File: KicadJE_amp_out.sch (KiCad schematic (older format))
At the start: 10 parts

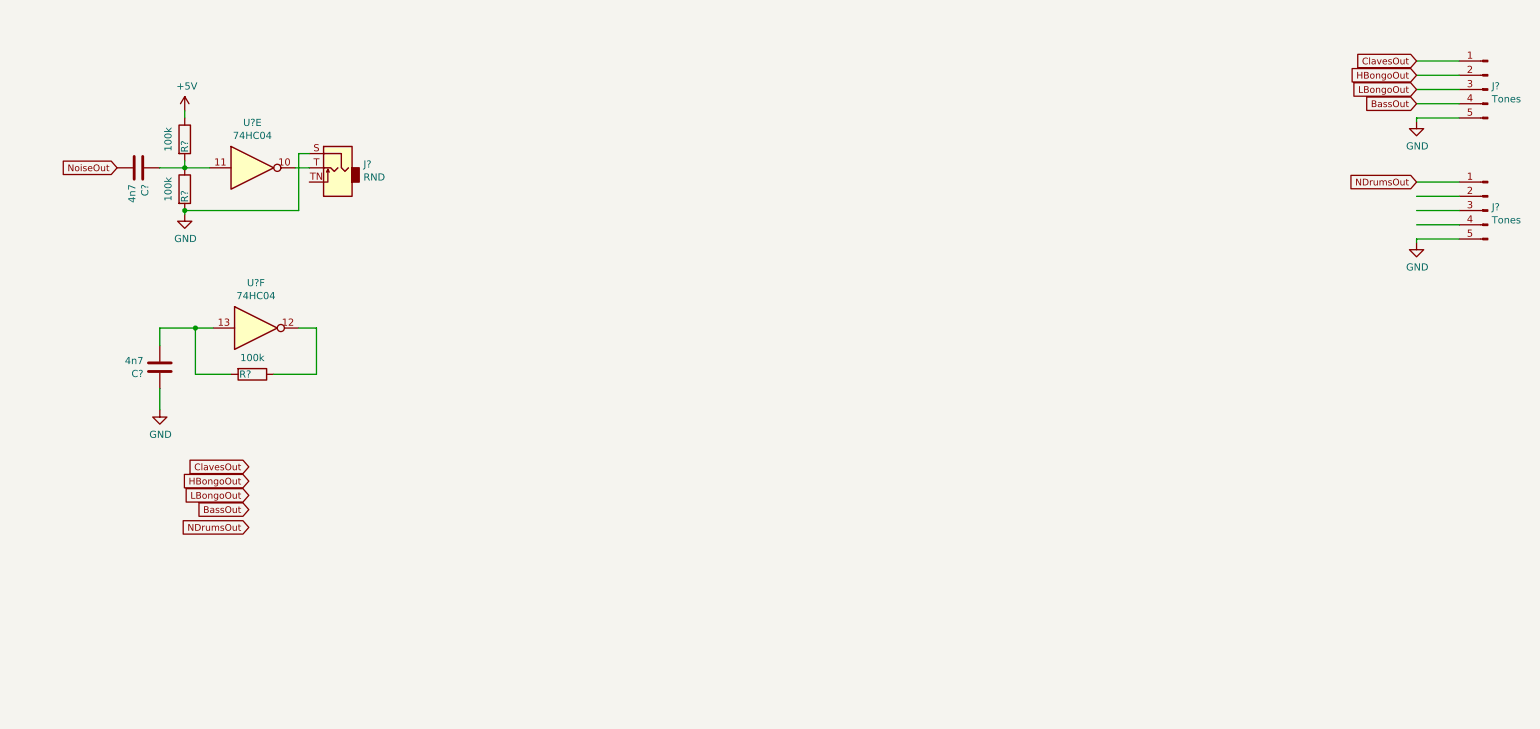
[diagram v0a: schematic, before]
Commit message: Amp out
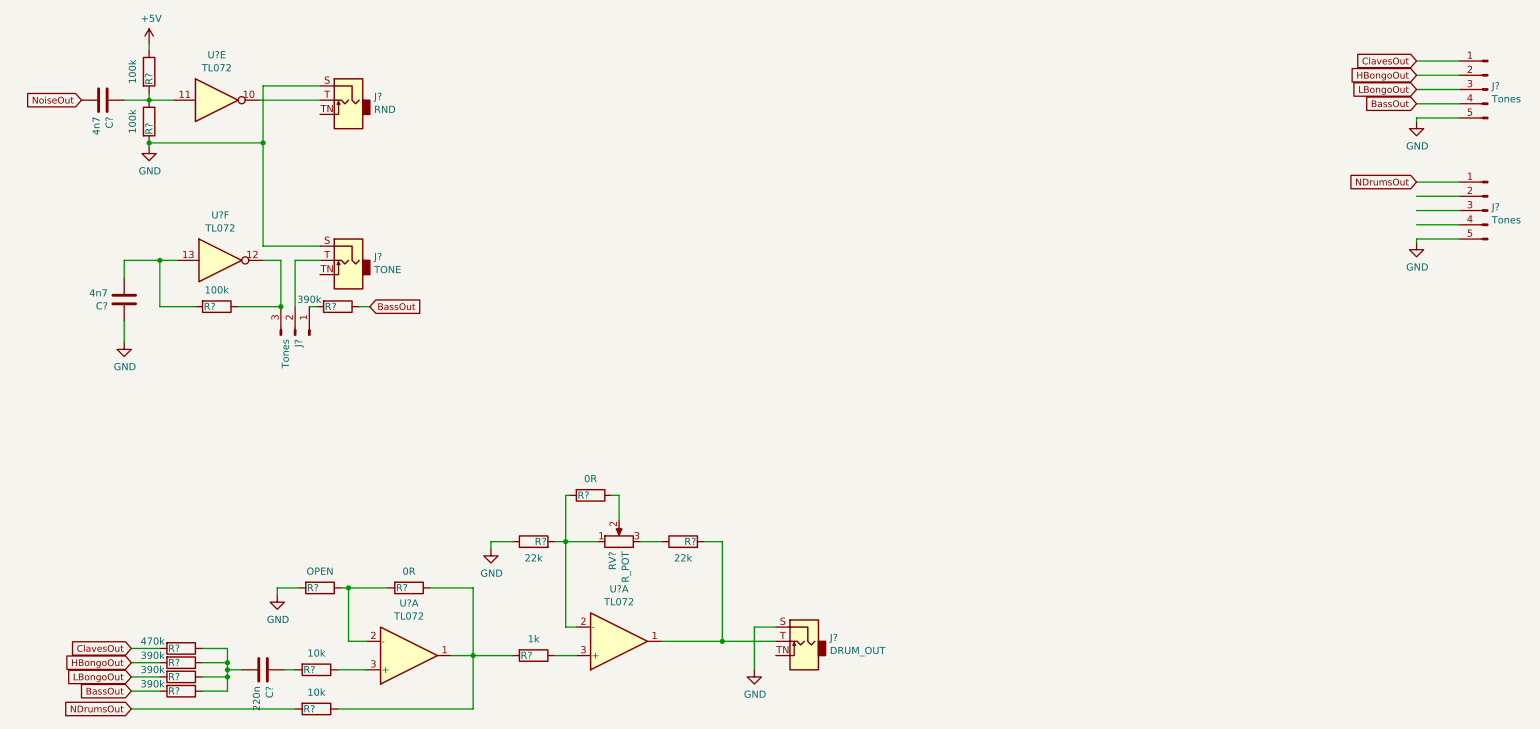
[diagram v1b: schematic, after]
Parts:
- added C?: 220n, Capacitor_SMD:C_1206_3216Metric_Pad1.42x1.75mm_HandSolder, symbol Device:C
- added J?: TONE, Connector_Audio:Jack_3.5mm_QingPu_WQP-PJ398SM_Vertical_CircularHoles, symbol Connector:AudioJack2_SwitchT
- added J?: Tones, Connector_PinHeader_2.54mm:PinHeader_1x03_P2.54mm_Vertical, symbol Connector:Conn_01x03_Male
- added J?: DRUM_OUT, Connector_Audio:Jack_3.5mm_QingPu_WQP-PJ398SM_Vertical_CircularHoles, symbol Connector:AudioJack2_SwitchT
- added R? (x4): 390k, AJ:R_0805_AJ, symbol Device:R
- added R?: 470k, AJ:R_0805_AJ, symbol Device:R
- added R? (x2): 10k, AJ:R_0805_AJ, symbol Device:R
- added R? (x2): 22k, AJ:R_0805_AJ, symbol Device:R
- added R?: 1k, AJ:R_0805_AJ, symbol Device:R
- added R? (x2): 0R, AJ:R_0805_AJ, symbol Device:R
- added R?: OPEN, AJ:R_0805_AJ, symbol Device:R
- added RV?: R_POT, AJ:Potentiometer_China_RK09_Single_Vertical_AJ, symbol Device:R_POT
- added U? (x2): TL072, AJ:AJ_SO-8_5.3x6.2mm_P1.27mm, symbol Amplifier_Operational:TL072
- U? (x2): value 74HC04 -> TL072; footprint (none) -> AJ:AJ_SO-8_5.3x6.2mm_P1.27mm
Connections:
- wire segments 30 -> 82
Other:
- moved on the sheet: C?, J?, R?, U?E, U?F

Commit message: sch amp
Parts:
- R?: value 390k -> 10k
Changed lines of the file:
@@
 Wire Wire Line
 	2425 2225 2600 2225
-Text GLabel 2950 2550 2    47   Input ~ 0
-BassOut
 $Comp
 L Device:C C?
@@
 AR Path="/6165D4D0/61BC62DE" Ref="R?"  Part="1"
 F 0 "R?" V 2725 2500 50  0000 C CNN
-F 1 "390k" V 2675 2350 50  0000 C CNN
+F 1 "10k" V 2675 2350 50  0000 C CNN
 F 2 "AJ:R_0805_AJ" V 2655 2550 50  0001 C CNN
 F 3 "~" H 2725 2550 50  0001 C CNN
@@
 Wire Wire Line
 	5650 4800 5650 5100
+Text GLabel 10300 1775 0    47   Input ~ 0
+NoiseOut
+Text GLabel 2950 2550 2    47   Input ~ 0
+NoiseOut
 $EndSCHEMATC

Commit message: Update misc diags
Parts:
- added R? (x3): 390k, AJ:R_0805_AJ, symbol Device:R
- added R?: 470k, AJ:R_0805_AJ, symbol Device:R
- added R? (x2): 10k, AJ:R_0805_AJ, symbol Device:R
- J?: value Tones -> Noise; footprint Connector_PinHeader_2.54mm:PinHeader_1x05_P2.54mm_Vertical -> Connector_PinHeader_2.54mm:PinHeader_1x03_P2.54mm_Vertical; symbol Connector:Conn_01x05_Male -> Connector:Conn_01x03_Male
- J?: value Tones -> Tone/Noise
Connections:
- net BassOut: now also R?.2; no longer J?.4 (Pin_4)
- net ClavesOut: now also R?.2; no longer J?.1 (Pin_1)
- net GND: now also J?.1 (Pin_1), J?.1 (Pin_1); no longer J?.5 (Pin_5), J?.5 (Pin_5)
- net HBongoOut: now also R?.2; no longer J?.2 (Pin_2)
- net LBongoOut: now also R?.2; no longer J?.3 (Pin_3)
- net NDrumsOut: now also R?.2; no longer J?.1 (Pin_1)
- net NoiseOut: now also R?.2; no longer J?.2 (Pin_2)
- net at J?.3 (Pin_3): now also R?.1
- new net: J?.4 (Pin_4), R?.1
- new net: J?.5 (Pin_5), R?.1
- new net: J?.3 (Pin_3), R?.1
- new net: J?.2 (Pin_2), R?.1 (x2)
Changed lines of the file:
@@
 F 3 "~" H 10800 1025 50  0001 C CNN
 	1    10800 1025
-	-1   0    0    -1
-$EndComp
-Text GLabel 10300 1025 0    47   Input ~ 0
+	-1   0    0    1
+$EndComp
+Text GLabel 9800 1025 0    47   Input ~ 0
 LBongoOut
-Text GLabel 10300 1125 0    47   Input ~ 0
+Text GLabel 9800 1125 0    47   Input ~ 0
 BassOut
-Text GLabel 10300 825  0    47   Input ~ 0
+Text GLabel 9800 825  0    47   Input ~ 0
 ClavesOut
-Text GLabel 10300 925  0    47   Input ~ 0
+Text GLabel 9800 925  0    47   Input ~ 0
 HBongoOut
 Wire Wire Line
@@
 	2325 2225 2200 2225
 $Comp
-L Connector:Conn_01x05_Male J?
+L Connector:Conn_01x03_Male J?
 U 1 1 61710EAB
-P 10800 1875
+P 10800 1775
 AR Path="/607E07E1/61710EAB" Ref="J?"  Part="1"
 AR Path="/61710EAB" Ref="J?"  Part="1"
 AR Path="/6165D4D0/61710EAB" Ref="J?"  Part="1"
-F 0 "J?" H 10772 1899 50  0000 R CNN
-F 1 "Tones" H 10772 1808 50  0000 R CNN
-F 2 "Connector_PinHeader_2.54mm:PinHeader_1x05_P2.54mm_Vertical" H 10800 1875 50  0001 C CNN
-F 3 "~" H 10800 1875 50  0001 C CNN
-	1    10800 1875
-	-1   0    0    -1
+F 0 "J?" V 10772 1799 50  0000 R CNN
+F 1 "Noise" H 10772 1708 50  0000 R CNN
+F 2 "Connector_PinHeader_2.54mm:PinHeader_1x03_P2.54mm_Vertical" H 10800 1775 50  0001 C CNN
+F 3 "~" H 10800 1775 50  0001 C CNN
+	1    10800 1775
+	-1   0    0    1
 $EndComp
 $Comp
 L power:GND #PWR?
 U 1 1 61715219
-P 10300 2100
+P 10300 1900
 AR Path="/61715219" Ref="#PWR?"  Part="1"
 AR Path="/6165D4D0/61715219" Ref="#PWR?"  Part="1"
-F 0 "#PWR?" H 10300 1850 50  0001 C CNN
-F 1 "GND" H 10305 1927 50  0000 C CNN
-F 2 "" H 10300 2100 50  0001 C CNN
-F 3 "" H 10300 2100 50  0001 C CNN
-	1    10300 2100
+F 0 "#PWR?" H 10300 1650 50  0001 C CNN
+F 1 "GND" H 10305 1727 50  0000 C CNN
+F 2 "" H 10300 1900 50  0001 C CNN
+F 3 "" H 10300 1900 50  0001 C CNN
+	1    10300 1900
 	1    0    0    -1
 $EndComp
 Wire Wire Line
-	10300 2100 10300 2075
-Wire Wire Line
-	10300 2075 10600 2075
-Text GLabel 10300 1675 0    47   Input ~ 0
+	10300 1900 10300 1875
+Text GLabel 9800 1675 0    47   Input ~ 0
 NDrumsOut
-Wire Wire Line
-	10600 1975 10300 1975
 Wire Wire Line
 	10300 1875 10600 1875
@@
 AR Path="/6165D4D0/61A8A423" Ref="J?"  Part="1"
 F 0 "J?" H 2397 2774 50  0000 R CNN
-F 1 "Tones" H 2397 2683 50  0000 R CNN
+F 1 "Tone/Noise" H 2397 2683 50  0000 R CNN
 F 2 "Connector_PinHeader_2.54mm:PinHeader_1x03_P2.54mm_Vertical" H 2425 2750 50  0001 C CNN
 F 3 "~" H 2425 2750 50  0001 C CNN
@@
 Wire Wire Line
 	5650 4800 5650 5100
-Text GLabel 10300 1775 0    47   Input ~ 0
+Text GLabel 9800 1775 0    47   Input ~ 0
 NoiseOut
 Text GLabel 2950 2550 2    47   Input ~ 0
 NoiseOut
+$Comp
+L Device:R R?
+U 1 1 608AC9E1
+P 10150 925
+AR Path="/608AC9E1" Ref="R?"  Part="1"
+AR Path="/5C8C5FC0/608AC9E1" Ref="R?"  Part="1"
+AR Path="/5D60ED9A/608AC9E1" Ref="R?"  Part="1"
+AR Path="/60565919/608AC9E1" Ref="R?"  Part="1"
+AR Path="/6165D4D0/608AC9E1" Ref="R?"  Part="1"
+F 0 "R?" V 10150 875 50  0000 C CNN
+F 1 "390k" V 10100 725 50  0000 C CNN
+F 2 "AJ:R_0805_AJ" V 10080 925 50  0001 C CNN
+F 3 "~" H 10150 925 50  0001 C CNN
+	1    10150 925
+	0    1    1    0
+$EndComp
+$Comp
+L Device:R R?
+U 1 1 608ACE07
+P 10150 825
+AR Path="/608ACE07" Ref="R?"  Part="1"
+AR Path="/5C8C5FC0/608ACE07" Ref="R?"  Part="1"
+AR Path="/5D60ED9A/608ACE07" Ref="R?"  Part="1"
+AR Path="/60565919/608ACE07" Ref="R?"  Part="1"
+AR Path="/6165D4D0/608ACE07" Ref="R?"  Part="1"
+F 0 "R?" V 10150 775 50  0000 C CNN
+F 1 "470k" V 10100 625 50  0000 C CNN
+F 2 "AJ:R_0805_AJ" V 10080 825 50  0001 C CNN
+F 3 "~" H 10150 825 50  0001 C CNN
+	1    10150 825
+	0    1    1    0
+$EndComp
+$Comp
+L Device:R R?
+U 1 1 608ACE11
+P 10150 1025
+AR Path="/608ACE11" Ref="R?"  Part="1"
+AR Path="/5C8C5FC0/608ACE11" Ref="R?"  Part="1"
+AR Path="/5D60ED9A/608ACE11" Ref="R?"  Part="1"
+AR Path="/60565919/608ACE11" Ref="R?"  Part="1"
+AR Path="/6165D4D0/608ACE11" Ref="R?"  Part="1"
+F 0 "R?" V 10150 975 50  0000 C CNN
+F 1 "390k" V 10100 825 50  0000 C CNN
+F 2 "AJ:R_0805_AJ" V 10080 1025 50  0001 C CNN
+F 3 "~" H 10150 1025 50  0001 C CNN
+	1    10150 1025
+	0    1    1    0
+$EndComp
+$Comp
+L Device:R R?
+U 1 1 608ACE1B
+P 10150 1125
+AR Path="/608ACE1B" Ref="R?"  Part="1"
+AR Path="/5C8C5FC0/608ACE1B" Ref="R?"  Part="1"
+AR Path="/5D60ED9A/608ACE1B" Ref="R?"  Part="1"
+AR Path="/60565919/608ACE1B" Ref="R?"  Part="1"
+AR Path="/6165D4D0/608ACE1B" Ref="R?"  Part="1"
+F 0 "R?" V 10150 1075 50  0000 C CNN
+F 1 "390k" V 10100 925 50  0000 C CNN
+F 2 "AJ:R_0805_AJ" V 10080 1125 50  0001 C CNN
+F 3 "~" H 10150 1125 50  0001 C CNN
+	1    10150 1125
+	0    1    1    0
+$EndComp
+Wire Wire Line
+	9800 825  10000 825
+Wire Wire Line
+	10000 1125 9800 1125
+Wire Wire Line
+	9800 1025 10000 1025
+Wire Wire Line
+	10000 925  9800 925
+$Comp
+L Device:R R?
+U 1 1 608B8687
+P 10150 1675
+AR Path="/608B8687" Ref="R?"  Part="1"
+AR Path="/5C8C5FC0/608B8687" Ref="R?"  Part="1"
+AR Path="/5D60ED9A/608B8687" Ref="R?"  Part="1"
+AR Path="/60565919/608B8687" Ref="R?"  Part="1"
+AR Path="/6165D4D0/608B8687" Ref="R?"  Part="1"
+F 0 "R?" V 10150 1625 50  0000 C CNN
+F 1 "10k" V 10100 1475 50  0000 C CNN
+F 2 "AJ:R_0805_AJ" V 10080 1675 50  0001 C CNN
+F 3 "~" H 10150 1675 50  0001 C CNN
+	1    10150 1675
+	0    1    1    0
+$EndComp
+$Comp
+L Device:R R?
+U 1 1 608B8FB9
+P 10150 1775
+AR Path="/608B8FB9" Ref="R?"  Part="1"
+AR Path="/5C8C5FC0/608B8FB9" Ref="R?"  Part="1"
+AR Path="/5D60ED9A/608B8FB9" Ref="R?"  Part="1"
+AR Path="/60565919/608B8FB9" Ref="R?"  Part="1"
+AR Path="/6165D4D0/608B8FB9" Ref="R?"  Part="1"
+F 0 "R?" V 10150 1725 50  0000 C CNN
+F 1 "10k" V 10100 1575 50  0000 C CNN
+F 2 "AJ:R_0805_AJ" V 10080 1775 50  0001 C CNN
+F 3 "~" H 10150 1775 50  0001 C CNN
+	1    10150 1775
+	0    1    1    0
+$EndComp
+Wire Wire Line
+	10000 1775 9800 1775
+Wire Wire Line
+	9800 1675 10000 1675
 $EndSCHEMATC

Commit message: Annotate
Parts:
- gave numbers to parts that had none: 35

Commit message: Footprint adj
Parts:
- U101: renamed from U301; value TL072 -> 74HC04; footprint AJ:AJ_SO-8_5.3x6.2mm_P1.27mm -> AJ:AJ_SO-14_5.3x6.2mm_P1.27mm
- renumbered U303 to U302
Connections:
- net at J304.T, R316.2: now also U302.7; no longer U302.1
- net at R313.2, R315.2, RV301.1: now also U302.6 (-); no longer U302.2 (-)
- net at R314.1: now also U302.5 (+); no longer U302.3 (+)
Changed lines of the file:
@@
 P 1875 1100
 AR Path="/61681728" Ref="U?"  Part="5"
-AR Path="/6165D4D0/61681728" Ref="U301"  Part="5"
-F 0 "U301" H 1875 1417 50  0000 C CNN
-F 1 "TL072" H 1875 1326 50  0000 C CNN
-F 2 "AJ:AJ_SO-8_5.3x6.2mm_P1.27mm" H 1875 1100 50  0001 C CNN
-F 3 "http://www.ti.com/lit/ds/symlink/tl071.pdf" H 1875 1100 50  0001 C CNN
+AR Path="/6165D4D0/61681728" Ref="U101"  Part="5"
+F 0 "U101" H 1875 1417 50  0000 C CNN
+F 1 "74HC04" H 1875 1326 50  0000 C CNN
+F 2 "AJ:AJ_SO-14_5.3x6.2mm_P1.27mm" H 1875 1100 50  0001 C CNN
+F 3 "" H 1875 1100 50  0001 C CNN
 	5    1875 1100
 	1    0    0    -1
@@
 P 1900 2225
 AR Path="/6168172E" Ref="U?"  Part="6"
-AR Path="/6165D4D0/6168172E" Ref="U301"  Part="6"
-F 0 "U301" H 1900 2542 50  0000 C CNN
-F 1 "TL072" H 1900 2451 50  0000 C CNN
-F 2 "AJ:AJ_SO-8_5.3x6.2mm_P1.27mm" H 1900 2225 50  0001 C CNN
-F 3 "http://www.ti.com/lit/ds/symlink/tl071.pdf" H 1900 2225 50  0001 C CNN
+AR Path="/6165D4D0/6168172E" Ref="U101"  Part="6"
+F 0 "U101" H 1900 2542 50  0000 C CNN
+F 1 "74HC04" H 1900 2451 50  0000 C CNN
+F 2 "AJ:AJ_SO-14_5.3x6.2mm_P1.27mm" H 1900 2225 50  0001 C CNN
+F 3 "" H 1900 2225 50  0001 C CNN
 	6    1900 2225
 	1    0    0    -1
@@
 	3675 5000 3525 5000
 $Comp
-L Amplifier_Operational:TL072 U303
-U 1 1 61BAEFD9
+L Amplifier_Operational:TL072 U302
+U 2 1 61BAEFD9
 P 4700 4900
-F 0 "U303" H 4700 4533 50  0000 C CNN
+F 0 "U302" H 4700 4533 50  0000 C CNN
 F 1 "TL072" H 4700 4624 50  0000 C CNN
 F 2 "AJ:AJ_SO-8_5.3x6.2mm_P1.27mm" H 4700 4900 50  0001 C CNN
 F 3 "http://www.ti.com/lit/ds/symlink/tl071.pdf" H 4700 4900 50  0001 C CNN
-	1    4700 4900
+	2    4700 4900
 	1    0    0    1
 $EndComp

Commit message: Faceplate etc
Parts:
- U101: footprint AJ:AJ_SO-14_5.3x6.2mm_P1.27mm -> Package_SO:SO-14_5.3x10.2mm_P1.27mm
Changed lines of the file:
@@
 F 0 "U101" H 1875 1417 50  0000 C CNN
 F 1 "74HC04" H 1875 1326 50  0000 C CNN
-F 2 "AJ:AJ_SO-14_5.3x6.2mm_P1.27mm" H 1875 1100 50  0001 C CNN
+F 2 "Package_SO:SO-14_5.3x10.2mm_P1.27mm" H 1875 1100 50  0001 C CNN
 F 3 "" H 1875 1100 50  0001 C CNN
 	5    1875 1100
@@
 F 0 "U101" H 1900 2542 50  0000 C CNN
 F 1 "74HC04" H 1900 2451 50  0000 C CNN
-F 2 "AJ:AJ_SO-14_5.3x6.2mm_P1.27mm" H 1900 2225 50  0001 C CNN
+F 2 "Package_SO:SO-14_5.3x10.2mm_P1.27mm" H 1900 2225 50  0001 C CNN
 F 3 "" H 1900 2225 50  0001 C CNN
 	6    1900 2225

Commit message: Powerfootprintupdated
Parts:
- removed R315: 0R, AJ:R_0805_AJ, symbol Device:R
- removed RV301: R_POT, AJ:Potentiometer_China_RK09_Single_Vertical_AJ, symbol Device:R_POT
- C301, C302, C303: footprint Capacitor_SMD:C_1206_3216Metric_Pad1.42x1.75mm_HandSolder -> AJ:C_0805_AJ
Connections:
- net at R313.2, U302.6 (-): now also R316.1
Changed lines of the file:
@@
 F 0 "C301" H 1190 1146 50  0000 L CNN
 F 1 "4n7" H 1190 1055 50  0000 L CNN
-F 2 "Capacitor_SMD:C_1206_3216Metric_Pad1.42x1.75mm_HandSolder" H 1113 950 50  0001 C CNN
+F 2 "AJ:C_0805_AJ" H 1113 950 50  0001 C CNN
 F 3 "~" H 1075 1100 50  0001 C CNN
 	1    1075 1100
@@
 F 0 "C302" H 1340 2546 50  0000 L CNN
 F 1 "4n7" H 1340 2455 50  0000 L CNN
-F 2 "Capacitor_SMD:C_1206_3216Metric_Pad1.42x1.75mm_HandSolder" H 1263 2350 50  0001 C CNN
+F 2 "AJ:C_0805_AJ" H 1263 2350 50  0001 C CNN
 F 3 "~" H 1225 2500 50  0001 C CNN
 	1    1225 2500
@@
 F 0 "C303" H 2315 5146 50  0000 L CNN
 F 1 "220n" H 2315 5055 50  0000 L CNN
-F 2 "Capacitor_SMD:C_1206_3216Metric_Pad1.42x1.75mm_HandSolder" H 2238 4950 50  0001 C CNN
+F 2 "AJ:C_0805_AJ" H 2238 4950 50  0001 C CNN
 F 3 "~" H 2200 5100 50  0001 C CNN
 	1    2200 5100
@@
 	0    -1   -1   0
 $EndComp
-$Comp
-L Device:R_POT RV301
-U 1 1 61BB7D8E
-P 4700 4200
-F 0 "RV301" H 4631 4246 50  0000 R CNN
-F 1 "R_POT" H 4631 4155 50  0000 R CNN
-F 2 "AJ:Potentiometer_China_RK09_Single_Vertical_AJ" H 4700 4200 50  0001 C CNN
-F 3 "~" H 4700 4200 50  0001 C CNN
-	1    4700 4200
-	0    -1   -1   0
-$EndComp
 Wire Wire Line
 	5425 4200 5300 4200
@@
 	4325 4800 4325 4200
 Wire Wire Line
-	4325 4200 4550 4200
-Wire Wire Line
-	4850 4200 5000 4200
-Wire Wire Line
 	4325 4200 4250 4200
-Connection ~ 4325 4200
 Wire Wire Line
 	5000 4900 5425 4900
@@
 	2300 4525 2450 4525
 $Comp
-L Device:R R?
-U 1 1 61BE0178
-P 4500 3875
-AR Path="/61BE0178" Ref="R?"  Part="1"
-AR Path="/5C8C5FC0/61BE0178" Ref="R?"  Part="1"
-AR Path="/5D60ED9A/61BE0178" Ref="R?"  Part="1"
-AR Path="/60565919/61BE0178" Ref="R?"  Part="1"
-AR Path="/6165D4D0/61BE0178" Ref="R315"  Part="1"
-F 0 "R315" V 4500 3825 50  0000 C CNN
-F 1 "0R" V 4384 3875 50  0000 C CNN
-F 2 "AJ:R_0805_AJ" V 4430 3875 50  0001 C CNN
-F 3 "~" H 4500 3875 50  0001 C CNN
-	1    4500 3875
-	0    1    1    0
-$EndComp
-Wire Wire Line
-	4700 4050 4700 3875
-Wire Wire Line
-	4700 3875 4650 3875
-Wire Wire Line
-	4325 3875 4325 4200
-Wire Wire Line
-	4350 3875 4325 3875
-$Comp
 L Connector:AudioJack2_SwitchT J?
 U 1 1 61BE2ABB
@@
 Wire Wire Line
 	9800 1675 10000 1675
+Wire Wire Line
+	4325 4200 5000 4200
+Connection ~ 4325 4200
 $EndSCHEMATC

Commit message: AC coupled noise
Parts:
- added C304: 220n, AJ:C_0805_AJ, symbol Device:C
- J303: value TONE -> Noise
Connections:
- net at J303.T: now also C304.1; no longer J301.2 (Pin_2)
- new net: C304.2, J301.2 (Pin_2)
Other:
- moved on the sheet: J302, J303
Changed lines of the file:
@@
 L Connector:AudioJack2_SwitchT J?
 U 1 1 61681759
-P 2800 1100
+P 3250 1100
 AR Path="/607E07E1/61681759" Ref="J?"  Part="1"
 AR Path="/61681759" Ref="J?"  Part="1"
 AR Path="/6165D4D0/61681759" Ref="J302"  Part="1"
-F 0 "J302" H 2620 1125 50  0000 R CNN
-F 1 "RND" H 2620 1034 50  0000 R CNN
-F 2 "Connector_Audio:Jack_3.5mm_QingPu_WQP-PJ398SM_Vertical_CircularHoles" H 2800 1100 50  0001 C CNN
-F 3 "~" H 2800 1100 50  0001 C CNN
-	1    2800 1100
+F 0 "J302" H 3070 1125 50  0000 R CNN
+F 1 "RND" H 3070 1034 50  0000 R CNN
+F 2 "Connector_Audio:Jack_3.5mm_QingPu_WQP-PJ398SM_Vertical_CircularHoles" H 3250 1100 50  0001 C CNN
+F 3 "~" H 3250 1100 50  0001 C CNN
+	1    3250 1100
 	-1   0    0    -1
 $EndComp
@@
 L Connector:AudioJack2_SwitchT J?
 U 1 1 61A8618F
-P 2800 2225
+P 3250 2225
 AR Path="/607E07E1/61A8618F" Ref="J?"  Part="1"
 AR Path="/61A8618F" Ref="J?"  Part="1"
 AR Path="/6165D4D0/61A8618F" Ref="J303"  Part="1"
-F 0 "J303" H 2620 2250 50  0000 R CNN
-F 1 "TONE" H 2620 2159 50  0000 R CNN
-F 2 "Connector_Audio:Jack_3.5mm_QingPu_WQP-PJ398SM_Vertical_CircularHoles" H 2800 2225 50  0001 C CNN
-F 3 "~" H 2800 2225 50  0001 C CNN
-	1    2800 2225
+F 0 "J303" H 3070 2250 50  0000 R CNN
+F 1 "Noise" H 3070 2159 50  0000 R CNN
+F 2 "Connector_Audio:Jack_3.5mm_QingPu_WQP-PJ398SM_Vertical_CircularHoles" H 3250 2225 50  0001 C CNN
+F 3 "~" H 3250 2225 50  0001 C CNN
+	1    3250 2225
 	-1   0    0    -1
 $EndComp
-Wire Wire Line
-	2200 1000 2600 1000
-Wire Wire Line
-	2175 1100 2600 1100
-Wire Wire Line
-	2600 2125 2200 2125
 Wire Wire Line
 	2200 2125 2200 1400
@@
 	4325 4200 5000 4200
 Connection ~ 4325 4200
+$Comp
+L Device:C C?
+U 1 1 6089BC96
+P 2750 2225
+AR Path="/6089BC96" Ref="C?"  Part="1"
+AR Path="/6165D4D0/6089BC96" Ref="C304"  Part="1"
+F 0 "C304" H 2865 2271 50  0000 L CNN
+F 1 "220n" H 2865 2180 50  0000 L CNN
+F 2 "AJ:C_0805_AJ" H 2788 2075 50  0001 C CNN
+F 3 "~" H 2750 2225 50  0001 C CNN
+	1    2750 2225
+	0    1    1    0
+$EndComp
+Wire Wire Line
+	2900 2225 3050 2225
+Wire Wire Line
+	2200 2125 3050 2125
+Wire Wire Line
+	2175 1100 3050 1100
+Wire Wire Line
+	2200 1000 3050 1000
 $EndSCHEMATC
